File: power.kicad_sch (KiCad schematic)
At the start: 0 parts

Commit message: Power layout
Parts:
- added BT1: Battery_Cell, symbol Device:Battery_Cell
- added C10, C11, C12, C7, C8, C9: C, symbol Device:C
- added D10, D11: D, symbol Device:D
- added D12, D9: LED, symbol Device:LED
- added J1: USB_C_Receptacle_PowerOnly_6P, symbol Connector:USB_C_Receptacle_PowerOnly_6P
- added L1: L, symbol Device:L
- added R18, R19, R20, R21, R22, R23, R24, R25: R, symbol Device:R
- added SW3: SW_Push, symbol Switch:SW_Push
- added U2: LM3670MF, Package_TO_SOT_SMD:TSOT-23-5, symbol Regulator_Switching:LM3670MF
- added U5: MCP73831-3-OT, Package_TO_SOT_SMD:SOT-23-5, symbol Battery_Management:MCP73831-3-OT
- added U6: MAX17043G+T, 21-0174B_MXM, symbol MAX17043:MAX17043G+T
- added U8: TS5A3159ADBVR, Package_TO_SOT_SMD:SOT-23-6, symbol Analog_Switch:TS5A3159ADBVR
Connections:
- new net: R25.1, SW3.1, U8.3
- new net: C10.1, R22.2, U6.2 (CELL)
- new net: J1.A5 (CC1), R24.1
- new net: D12.1 (K), R20.1
- new net: D9.1 (K), R19.1
- new net: R18.1, U5.5 (PROG)
- new net: U2.3 (EN), U8.4
- new net: L1.1, U2.5 (SW)
- new net: R19.2, U5.1 (STAT)
- new net: J1.B5 (CC2), R23.1
- new net FuelGage_LOW: R21.2, U6.5 (*ALRT)
- new net FuelGage_SCL: U6.7 (SCL)
- new net FuelGage_SDA: U6.8 (SDA)
- new net GND: BT1.2 (-), C10.2, C11.2, C12.2, C7.2, C8.2, C9.2, J1.A12 (GND), J1.B12 (GND), R18.2, R20.2, R23.2, R24.2, R25.2, U2.2 (GND), U5.2 (V_{SS}), U6.1 (CTG), U6.4 (GND), U6.6 (QSRT), U6.9 (EPAD)
- new net POWER_ON: U8.6
- new net VBAT: BT1.1 (+), C8.1, D11.2 (A), R22.1, U5.3 (V_{BAT})
- new net VBUS: C9.1, D10.2 (A), J1.A9 (VBUS), J1.B9 (VBUS), U5.4 (V_{DD})
- new net VCC: C11.1, D12.2 (A), L1.2, R21.1, U2.4 (FB), U6.3 (VDD)
- new net VIN: C12.1, C7.1, D10.1 (K), D11.1 (K), D9.2 (A), SW3.2, U2.1 (Vin), U8.1
- no-connect marks 0 -> 1

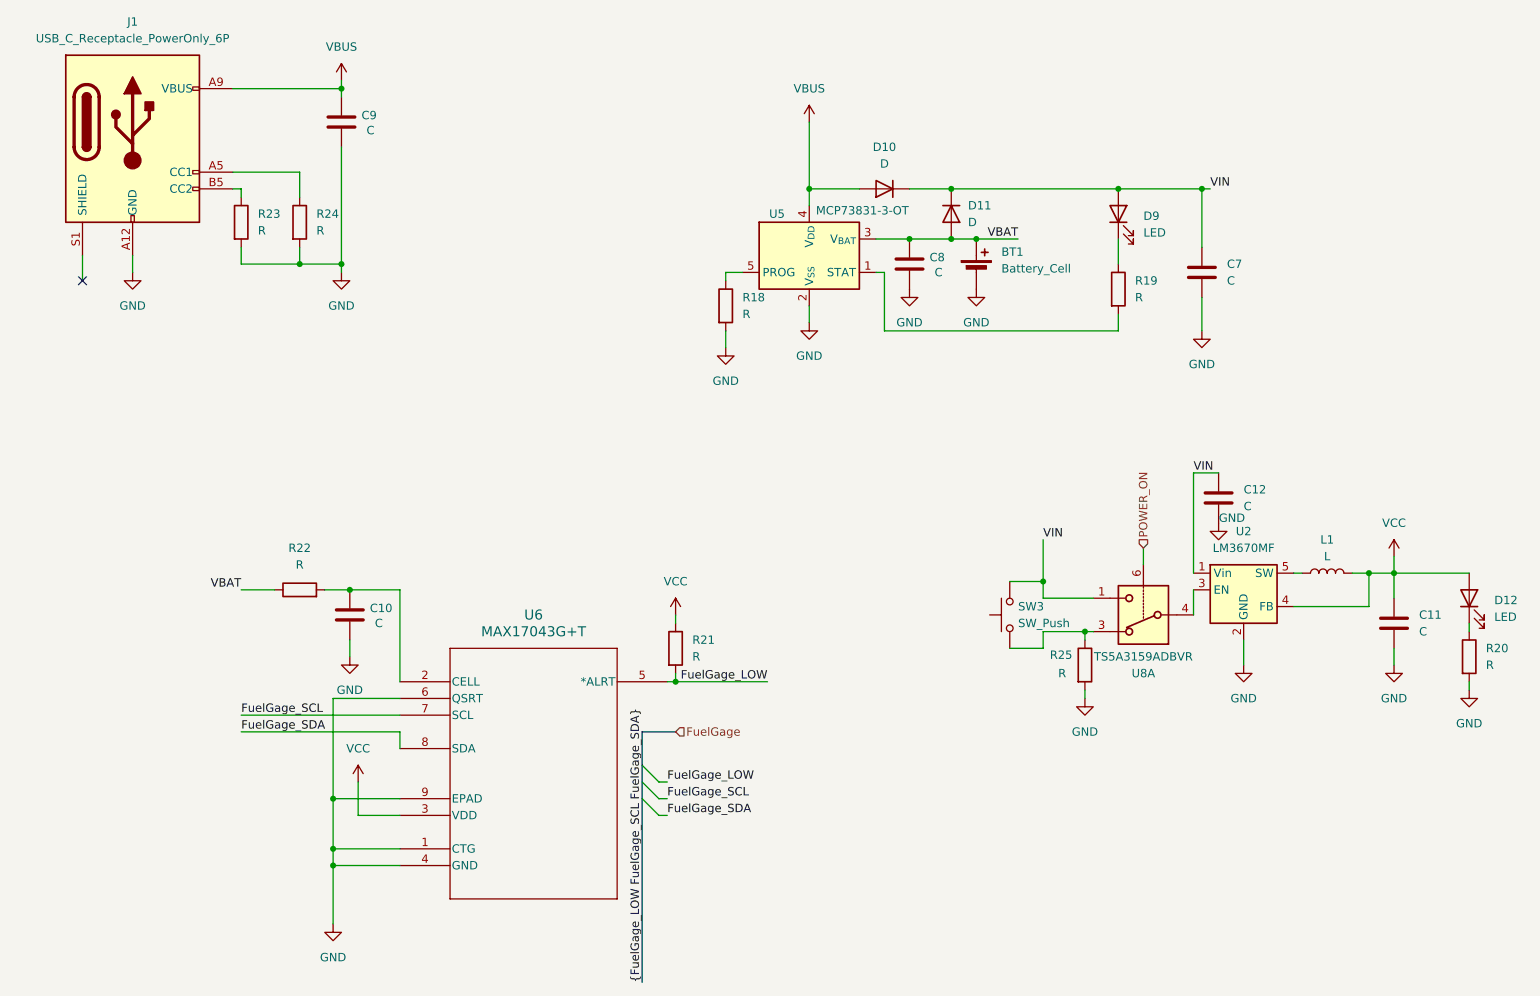
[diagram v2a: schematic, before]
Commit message: Controller wiring and schematic semantics
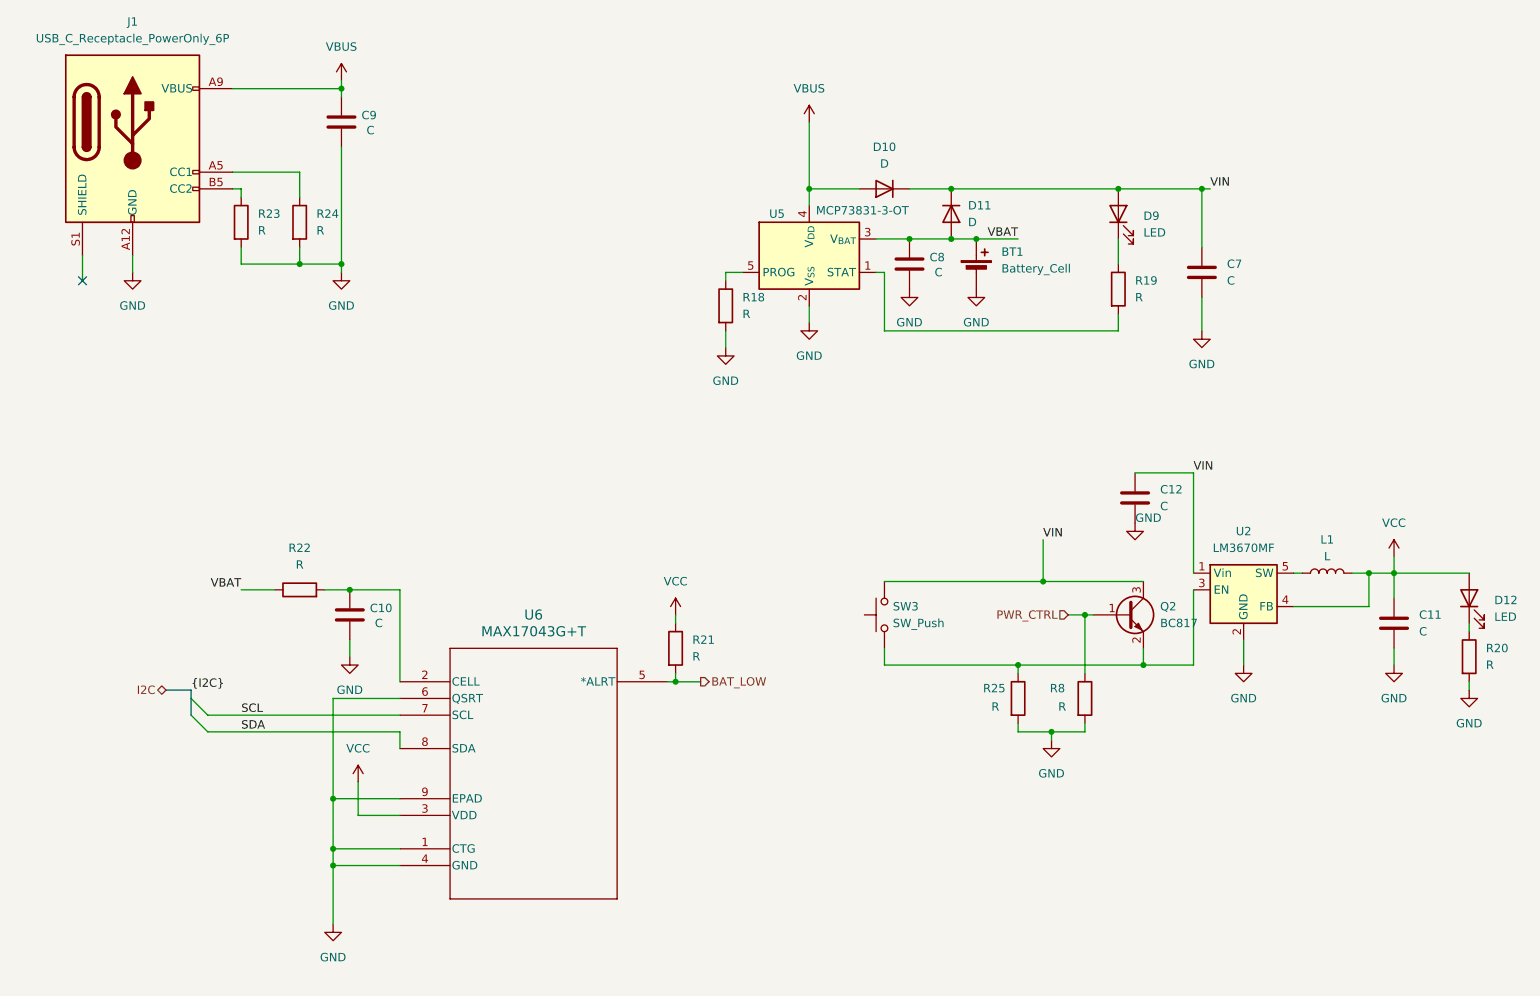
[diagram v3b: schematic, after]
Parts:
- removed U8: TS5A3159ADBVR, Package_TO_SOT_SMD:SOT-23-6, symbol Analog_Switch:TS5A3159ADBVR
- added Q2: BC817, Package_TO_SOT_SMD:SOT-23, symbol Transistor_BJT:BC817
- added R8: R, symbol Device:R
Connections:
- net GND: now also R8.2
- net VIN: now also Q2.3 (C)
- net at R25.1, SW3.1: now also U2.3 (EN), Q2.2 (E)
- net FuelGage_LOW renamed BAT_LOW
- net FuelGage_SCL renamed SCL
- net FuelGage_SDA renamed SDA
- new net PWR_CTRL: Q2.1 (B), R8.1
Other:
- moved on the sheet: C12, R25, SW3

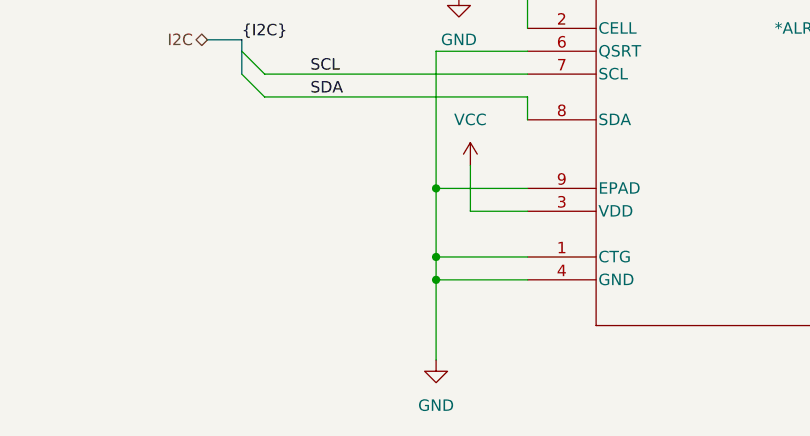
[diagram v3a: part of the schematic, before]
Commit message: Decoupling caps for ICs
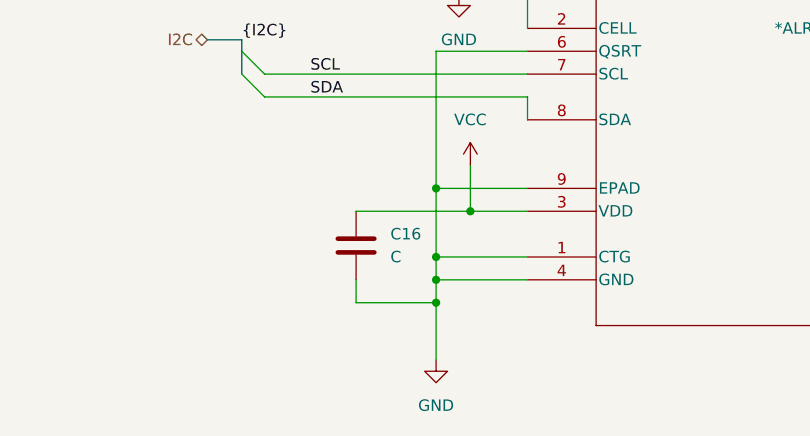
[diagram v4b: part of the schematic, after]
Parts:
- added C16: C, symbol Device:C
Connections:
- net GND: now also C16.2
- net VCC: now also C16.1
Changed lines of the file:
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@@
+	)
+	(junction
+		(at 80.01 171.45)
+		(diameter 0)
+		(color 0 0 0 0)
 	)
 	(junction
@@
 		(color 0 0 0 0)
 	)
+	(junction
+		(at 83.82 161.29)
+		(diameter 0)
+		(color 0 0 0 0)
+	)
 	(no_connect
 		(at 41.91 80.01)
@@
 	(wire
 		(pts
+			(xy 71.12 168.91) (xy 71.12 171.45)
+		)
+		(stroke
+			(width 0)
+			(type default)
+		)
+	)
+	(wire
+		(pts
 			(xy 163.83 87.63) (xy 163.83 78.74)
 		)
@@
 	(wire
 		(pts
+			(xy 71.12 161.29) (xy 83.82 161.29)
+		)
+		(stroke
+			(width 0)
+			(type default)
+		)
+	)
+	(wire
+		(pts
 			(xy 189.23 148.59) (xy 194.31 148.59)
 		)
@@
 	(wire
 		(pts
+			(xy 71.12 171.45) (xy 80.01 171.45)
+		)
+		(stroke
+			(width 0)
+			(type default)
+		)
+	)
+	(wire
+		(pts
 			(xy 90.17 158.75) (xy 80.01 158.75)
 		)
@@
 	(wire
 		(pts
-			(xy 80.01 168.91) (xy 80.01 177.8)
+			(xy 80.01 168.91) (xy 80.01 171.45)
 		)
 		(stroke
@@
 		(pts
 			(xy 194.31 147.32) (xy 194.31 148.59)
+		)
+		(stroke
+			(width 0)
+			(type default)
+		)
+	)
+	(wire
+		(pts
+			(xy 80.01 171.45) (xy 80.01 177.8)
 		)
 		(stroke
@@
 					(unit 1)
 				)
+			)
+		)
+	)
+	(symbol
+		(lib_id "Device:C")
+		(at 71.12 165.1 0)
+		(unit 1)
+		(exclude_from_sim no)
+		(in_bom yes)
+		(on_board yes)
+		(dnp no)
+		(fields_autoplaced yes)
+		(property "Reference" "C16"
+			(at 74.93 163.8299 0)
+			(effects
+				(font
+					(size 1.27 1.27)
+				)
+				(justify left)
+			)
+		)
+		(property "Value" "C"
+			(at 74.93 166.3699 0)
+			(effects
+				(font
+					(size 1.27 1.27)
+				)
+				(justify left)
+			)
+		)
+		(property "Footprint" ""
+			(at 72.0852 168.91 0)
+			(effects
+				(font
+					(size 1.27 1.27)
+				)
+				(hide yes)
+			)
+		)
+		(property "Datasheet" "~"
+			(at 71.12 165.1 0)
+			(effects
+				(font
+					(size 1.27 1.27)
+				)
+				(hide yes)
+			)
+		)
+		(property "Description" "Unpolarized capacitor"
+			(at 71.12 165.1 0)
+			(effects
+				(font
+					(size 1.27 1.27)
+				)
+				(hide yes)
+			)
+		)
+		(pin "1"
+		)
+		(pin "2"
+		)
+		(instances
+			(project "LifeCounter"
+				(path "/16b3e55a-9d75-49bf-a6fe-25414eb3d7da/8f87360a-db94-4899-a1b3-392efb8a6c91"
+					(reference "C16")
+					(unit 1)
+				)

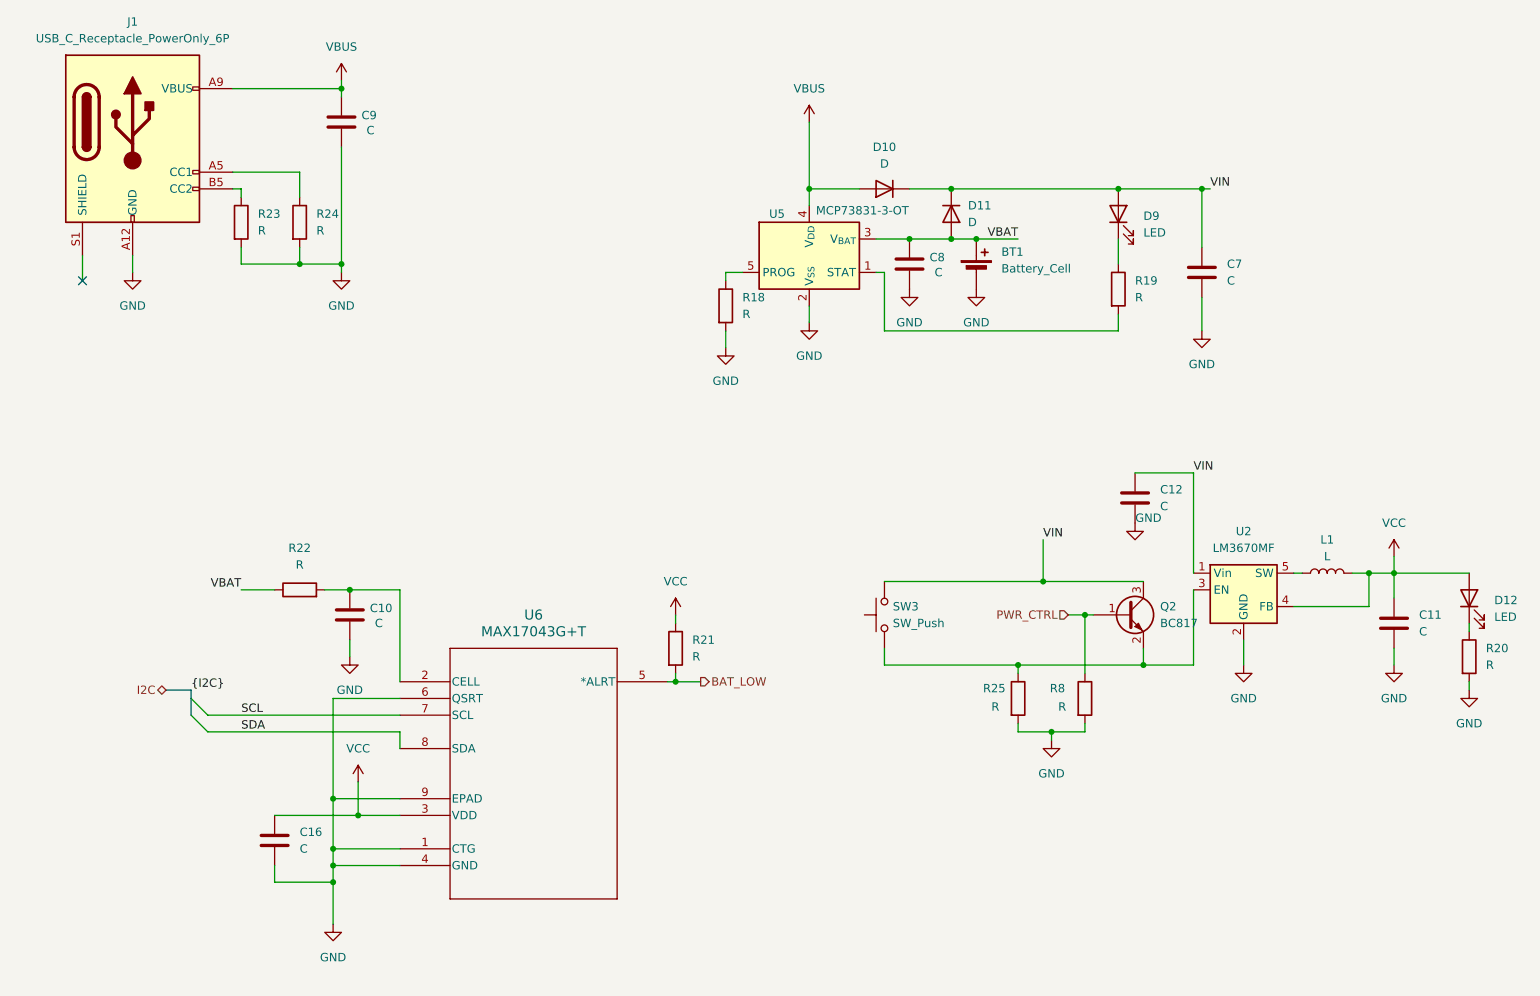
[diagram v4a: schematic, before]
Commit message: LED descriptions - Status LEDs could use some more work
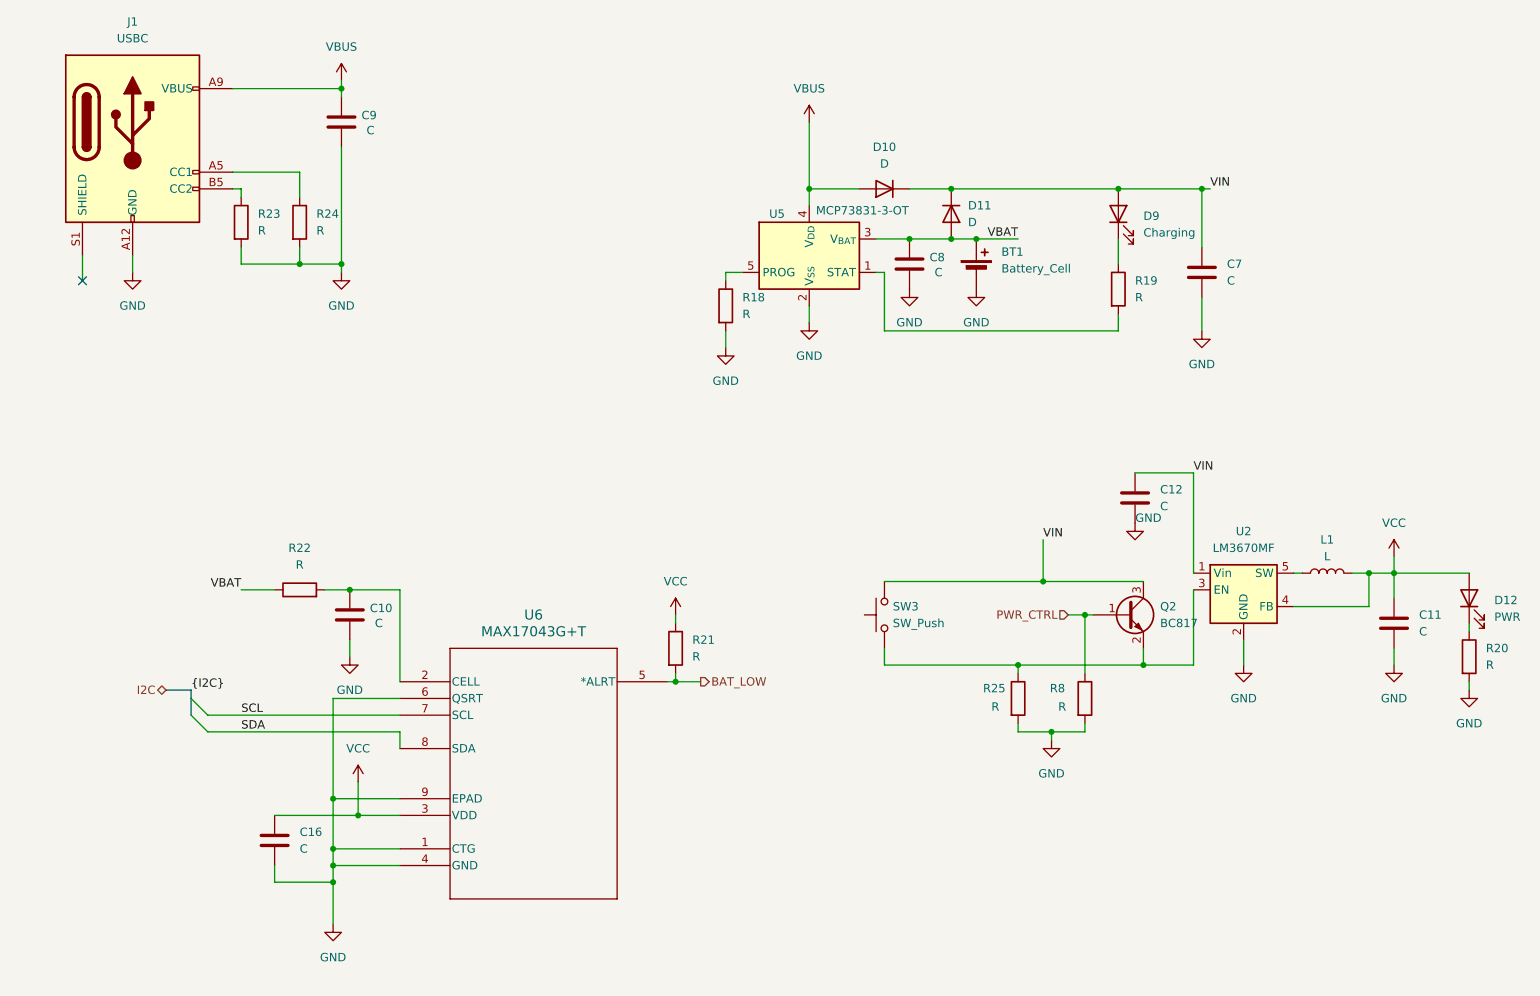
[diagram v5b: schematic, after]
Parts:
- D12: value LED -> PWR
- D9: value LED -> Charging
- J1: value USB_C_Receptacle_PowerOnly_6P -> USBC
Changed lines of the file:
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@@
 			)
 		)
-		(property "Value" "LED"
+		(property "Value" "PWR"
 			(at 256.54 131.1274 90)
 			(effects
@@
 			)
 		)
-		(property "Value" "LED"
+		(property "Value" "Charging"
 			(at 203.2 72.7074 90)
 			(effects
@@
 			)
 		)
-		(property "Value" "USB_C_Receptacle_PowerOnly_6P"
+		(property "Value" "USBC"
 			(at 49.53 43.18 0)
 			(effects
